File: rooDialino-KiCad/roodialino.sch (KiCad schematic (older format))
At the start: 49 parts, among them J1 Raspi Connector, J2 ICSP, J3 FTDI, J4 IR Receiver, J5 IR LED, Q1 2N7002, Q2 2N7002, Q3 2N7002, SW1 SW_Push, U1 ATmega328P, U2 TSOP312xx, U3 TXS0108EPW, Y1 16MHz

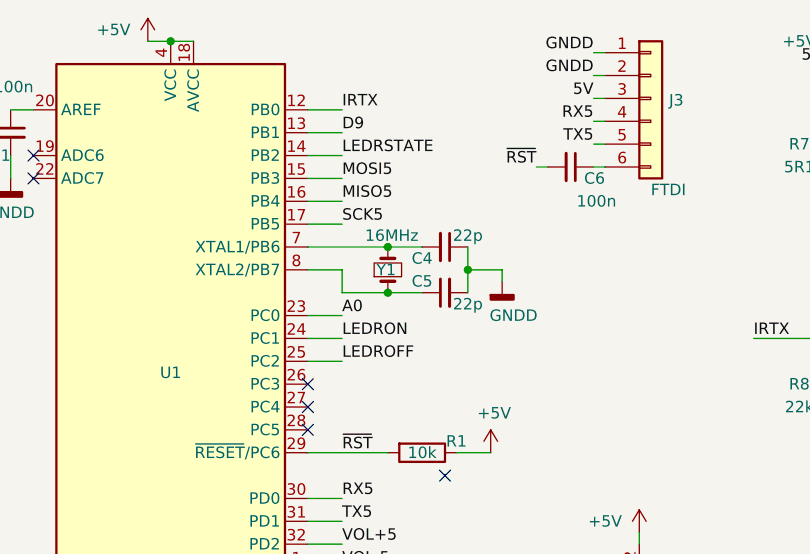
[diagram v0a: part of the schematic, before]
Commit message: Fixing the crystal footprint
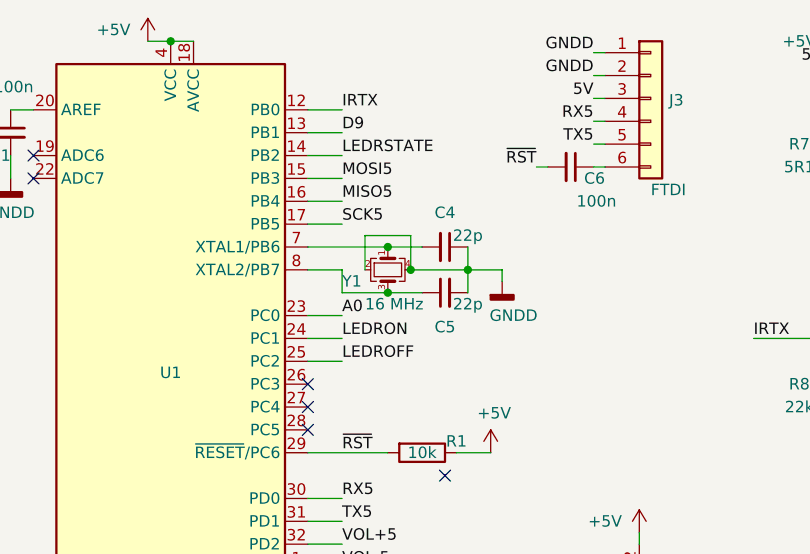
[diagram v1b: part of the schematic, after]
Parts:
- removed Y1: 16MHz, Crystal:Crystal_SMD_3225-4Pin_3.2x2.5mm, symbol Device:Crystal_Small
- added Y1: 16 MHz, Crystal:Crystal_SMD_3225-4Pin_3.2x2.5mm, symbol Device:Crystal_GND24_Small
- C11: LCSC (none) -> C1622
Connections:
- net GNDD: now also Y1.2, Y1.4
- net at C4.2, U1.7 (XTAL1/PB6): now also Y1.1
- net at C5.1, U1.8 (XTAL2/PB7): now also Y1.3
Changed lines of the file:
@@
 Wire Wire Line
 	700  1100 800  1100
-$Comp
-L Device:Crystal_Small Y1
-U 1 1 5E11C8C9
-P 2350 1800
-F 0 "Y1" V 2350 1750 50  0000 L CNN
-F 1 "16MHz" V 2500 1700 50  0000 L CNN
-F 2 "Crystal:Crystal_SMD_3225-4Pin_3.2x2.5mm" H 2350 1800 50  0001 C CNN
-F 3 "~" H 2350 1800 50  0001 C CNN
-F 4 "C13738" V 2350 1800 50  0001 C CNN "LCSC"
-	1    2350 1800
-	0    1    -1   0
-$EndComp
-Wire Wire Line
-	2000 1700 2350 1700
-Wire Wire Line
-	2350 1700 2500 1700
-Connection ~ 2350 1700
 Wire Wire Line
 	2700 1700 2700 1800
 Wire Wire Line
-	2350 1900 2500 1900
-Wire Wire Line
 	2000 1800 2150 1800
 Wire Wire Line
 	2150 1800 2150 1900
-Wire Wire Line
-	2150 1900 2350 1900
-Connection ~ 2350 1900
 $Comp
 L Device:C_Small C4
 U 1 1 5E11A53A
 P 2600 1700
-F 0 "C4" V 2650 1600 50  0000 C CNN
+F 0 "C4" V 2450 1700 50  0000 C CNN
 F 1 "22p" V 2550 1800 50  0000 C CNN
 F 2 "Capacitor_SMD:C_0402_1005Metric" H 2600 1700 50  0001 C CNN
@@
 U 1 1 5E11B014
 P 2600 1900
-F 0 "C5" V 2550 2000 50  0000 C CNN
+F 0 "C5" V 2750 1900 50  0000 C CNN
 F 1 "22p" V 2650 1800 50  0000 C CNN
 F 2 "Capacitor_SMD:C_0402_1005Metric" H 2600 1900 50  0001 C CNN
@@
 F 2 "Capacitor_SMD:C_0603_1608Metric" H 6050 6900 50  0001 C CNN
 F 3 "~" H 6050 6900 50  0001 C CNN
+F 4 "C1622" H 6050 6900 50  0001 C CNN "LCSC"
 	1    6050 6900
 	-1   0    0    1
@@
 NoConn ~ 2000 2500
 NoConn ~ 2600 2700
+$Comp
+L Device:Crystal_GND24_Small Y1
+U 1 1 617082D2
+P 2350 1800
+F 0 "Y1" V 2400 1600 50  0000 L CNN
+F 1 "16 MHz" V 2500 1700 50  0000 L CNN
+F 2 "Crystal:Crystal_SMD_3225-4Pin_3.2x2.5mm" H 2350 1800 50  0001 C CNN
+F 3 "~" H 2350 1800 50  0001 C CNN
+F 4 "C13738" V 2350 1800 50  0001 C CNN "LCSC"
+	1    2350 1800
+	0    1    1    0
+$EndComp
+Wire Wire Line
+	2150 1900 2350 1900
+Wire Wire Line
+	2000 1700 2350 1700
+Connection ~ 2350 1700
+Wire Wire Line
+	2350 1700 2500 1700
+Connection ~ 2350 1900
+Wire Wire Line
+	2350 1900 2500 1900
+Wire Wire Line
+	2700 1800 2450 1800
+Wire Wire Line
+	2250 1800 2250 1650
+Wire Wire Line
+	2250 1650 2450 1650
+Wire Wire Line
+	2450 1650 2450 1800
+Connection ~ 2450 1800
 $EndSCHEMATC

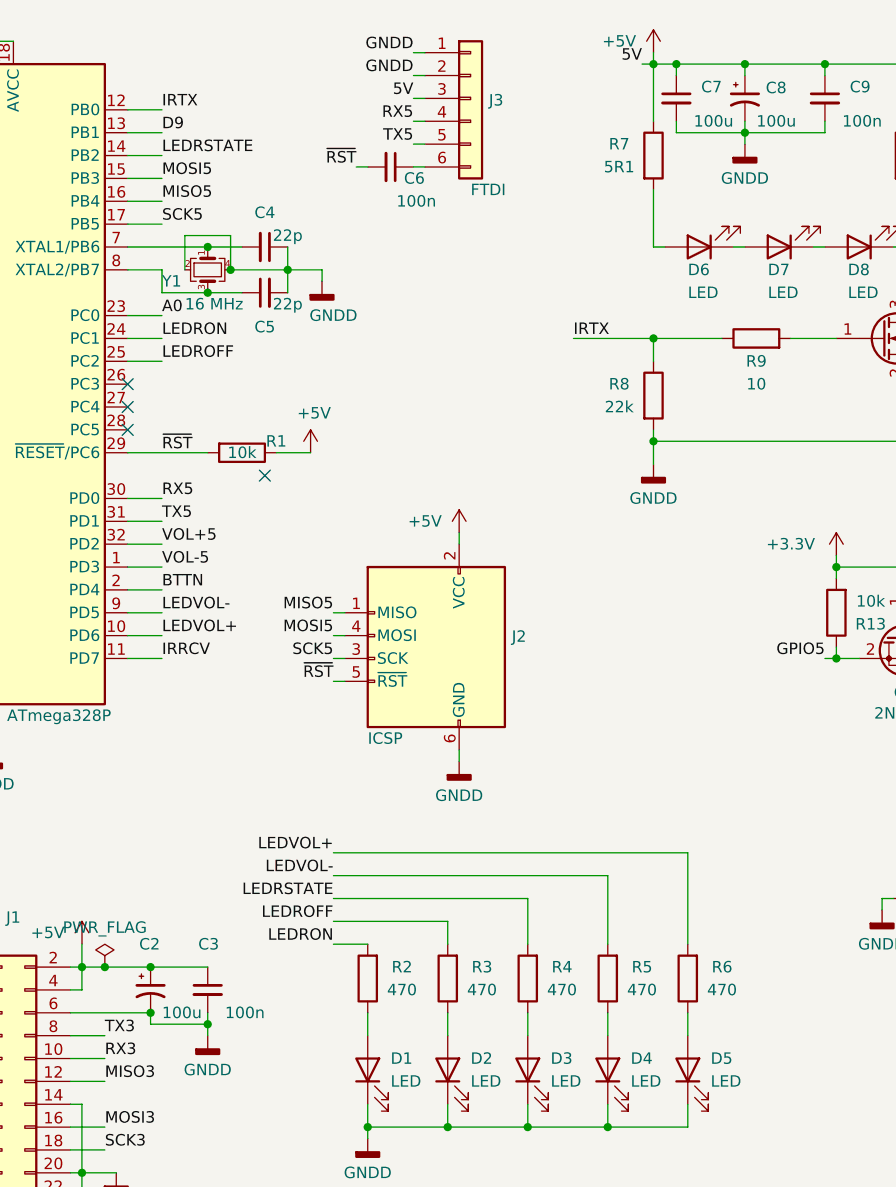
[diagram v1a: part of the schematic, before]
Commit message: Better caps, less magic smoke!
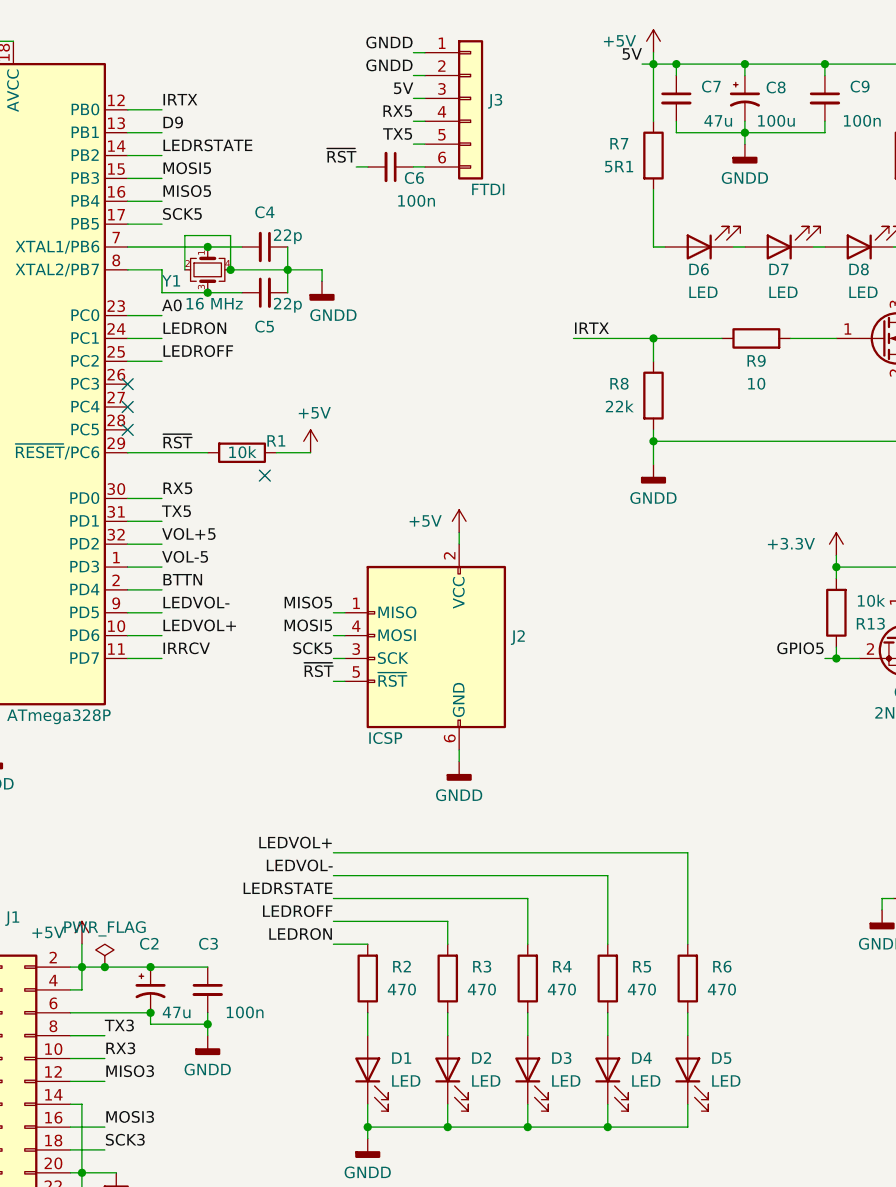
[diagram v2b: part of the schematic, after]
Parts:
- C2: value 100u -> 47u; footprint Capacitor_SMD:C_1210_3225Metric -> Capacitor_SMD:CP_Elec_4x5.8; LCSC C16133 -> C178589
- C7: value 100u -> 47u
- C8: footprint Capacitor_SMD:C_1210_3225Metric -> Capacitor_SMD:CP_Elec_4x5.8; LCSC C16133 -> C178589
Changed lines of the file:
@@
 F 0 "C8" H 4791 1096 50  0000 L CNN
 F 1 "100u" H 4750 950 50  0000 L CNN
-F 2 "Capacitor_SMD:C_1210_3225Metric" H 4700 1050 50  0001 C CNN
-F 3 "~" H 4700 1050 50  0001 C CNN
-F 4 "C16133" H 4700 1050 50  0001 C CNN "LCSC"
+F 2 "Capacitor_SMD:CP_Elec_4x5.8" H 4700 1050 50  0001 C CNN
+F 3 "https://lcsc.com/product-detail/Aluminum-Electrolytic-Capacitors---SMD_PANASONIC-EEEFT1C470AR_C178589.html" H 4700 1050 50  0001 C CNN
+F 4 "C178589" H 4700 1050 50  0001 C CNN "LCSC"
 	1    4700 1050
 	1    0    0    -1
@@
 P 2100 4950
 F 0 "C2" H 2050 5150 50  0000 L CNN
-F 1 "100u" H 2150 4850 50  0000 L CNN
-F 2 "Capacitor_SMD:C_1210_3225Metric" H 2100 4950 50  0001 C CNN
-F 3 "~" H 2100 4950 50  0001 C CNN
-F 4 "C16133" H 2100 4950 50  0001 C CNN "LCSC"
+F 1 "47u" H 2150 4850 50  0000 L CNN
+F 2 "Capacitor_SMD:CP_Elec_4x5.8" H 2100 4950 50  0001 C CNN
+F 3 "https://lcsc.com/product-detail/Aluminum-Electrolytic-Capacitors---SMD_PANASONIC-EEEFT1C470AR_C178589.html" H 2100 4950 50  0001 C CNN
+F 4 "C178589" H 2100 4950 50  0001 C CNN "LCSC"
 	1    2100 4950
 	1    0    0    -1
@@
 P 4400 1050
 F 0 "C7" H 4600 1100 50  0000 R CNN
-F 1 "100u" H 4650 950 50  0000 R CNN
+F 1 "47u" H 4650 950 50  0000 R CNN
 F 2 "Capacitor_SMD:C_1206_3216Metric" H 4400 1050 50  0001 C CNN
-F 3 "~" H 4400 1050 50  0001 C CNN
+F 3 "https://datasheet.lcsc.com/lcsc/1810301816_Samsung-Electro-Mechanics-CL31A107MQHNNNE_C15008.pdf" H 4400 1050 50  0001 C CNN
 F 4 "C15008" H 4400 1050 50  0001 C CNN "LCSC"
 	1    4400 1050

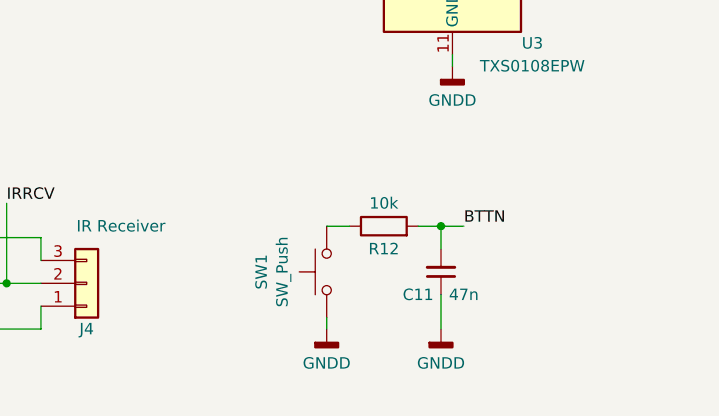
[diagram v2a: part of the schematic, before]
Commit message: Removing debounce RC
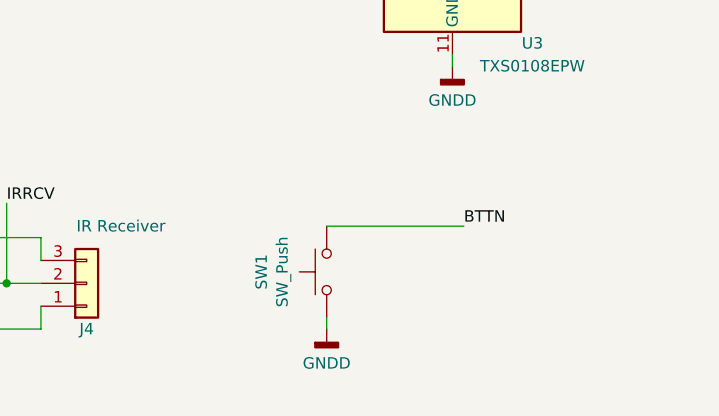
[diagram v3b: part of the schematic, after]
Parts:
- removed C11: 47n, Capacitor_SMD:C_0603_1608Metric, symbol Device:C_Small
- removed R12: 10k, Resistor_SMD:R_0402_1005Metric, symbol Device:R
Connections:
- net BTTN: now also SW1.2
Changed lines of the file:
@@
 VOL+5
-$Comp
-L Device:R R12
-U 1 1 6169CA12
-P 5800 6700
-F 0 "R12" V 5700 6700 50  0000 C CNN
-F 1 "10k" V 5900 6700 50  0000 C CNN
-F 2 "Resistor_SMD:R_0402_1005Metric" V 5730 6700 50  0001 C CNN
-F 3 "~" H 5800 6700 50  0001 C CNN
-F 4 "C25744" V 5800 6700 50  0001 C CNN "LCSC"
-	1    5800 6700
-	0    -1   -1   0
-$EndComp
-$Comp
-L Device:C_Small C11
-U 1 1 6169CEA6
-P 6050 6900
-F 0 "C11" H 6150 7000 50  0000 C CNN
-F 1 "47n" H 5950 7000 50  0000 C CNN
-F 2 "Capacitor_SMD:C_0603_1608Metric" H 6050 6900 50  0001 C CNN
-F 3 "~" H 6050 6900 50  0001 C CNN
-F 4 "C1622" H 6050 6900 50  0001 C CNN "LCSC"
-	1    6050 6900
-	-1   0    0    1
-$EndComp
-$Comp
-L power:GNDD #PWR023
-U 1 1 6169EC89
-P 6050 7150
-F 0 "#PWR023" H 6050 6900 50  0001 C CNN
-F 1 "GNDD" H 6050 7000 50  0000 C CNN
-F 2 "" H 6050 7150 50  0001 C CNN
-F 3 "" H 6050 7150 50  0001 C CNN
-	1    6050 7150
-	1    0    0    -1
-$EndComp
-Wire Wire Line
-	5950 6700 6050 6700
-Wire Wire Line
-	6050 6700 6050 6800
 $Comp
 L Switch:SW_Push SW1
@@
 $EndComp
 Wire Wire Line
-	5550 6700 5650 6700
-Wire Wire Line
-	6050 7000 6050 7150
-Wire Wire Line
 	5550 7150 5550 7100
 $Comp
@@
 F 1 "LED" V 3000 5200 50  0000 R CNN
 F 2 "LED_SMD:LED_0603_1608Metric" H 3050 5300 50  0001 C CNN
-F 3 "~" H 3050 5300 50  0001 C CNN
+F 3 "https://datasheet.lcsc.com/lcsc/1811101510_Everlight-Elec-19-217-BHC-ZL1M2RY-3T_C72041.pdf" H 3050 5300 50  0001 C CNN
 F 4 "C72041" V 3050 5300 50  0001 C CNN "LCSC"
 	1    3050 5300
@@
 F 1 "LED" V 3350 5200 50  0000 R CNN
 F 2 "LED_SMD:LED_0603_1608Metric" H 3400 5300 50  0001 C CNN
-F 3 "~" H 3400 5300 50  0001 C CNN
+F 3 "https://datasheet.lcsc.com/lcsc/1811101510_Everlight-Elec-19-217-BHC-ZL1M2RY-3T_C72041.pdf" H 3400 5300 50  0001 C CNN
 F 4 "C72041" V 3400 5300 50  0001 C CNN "LCSC"
 	1    3400 5300
@@
 F 1 "LED" V 3700 5200 50  0000 R CNN
 F 2 "LED_SMD:LED_0603_1608Metric" H 3750 5300 50  0001 C CNN
-F 3 "~" H 3750 5300 50  0001 C CNN
+F 3 "https://datasheet.lcsc.com/lcsc/1811101510_Everlight-Elec-19-217-BHC-ZL1M2RY-3T_C72041.pdf" H 3750 5300 50  0001 C CNN
 F 4 "C72041" V 3750 5300 50  0001 C CNN "LCSC"
 	1    3750 5300
@@
 Text Label 6150 6700 0    50   ~ 0
 BTTN
-Wire Wire Line
-	6150 6700 6050 6700
-Connection ~ 6050 6700
 Text Label 1100 6250 2    50   ~ 0
 GPIO5
@@
 	2450 1650 2450 1800
 Connection ~ 2450 1800
+Wire Wire Line
+	5550 6700 6150 6700
 $EndSCHEMATC

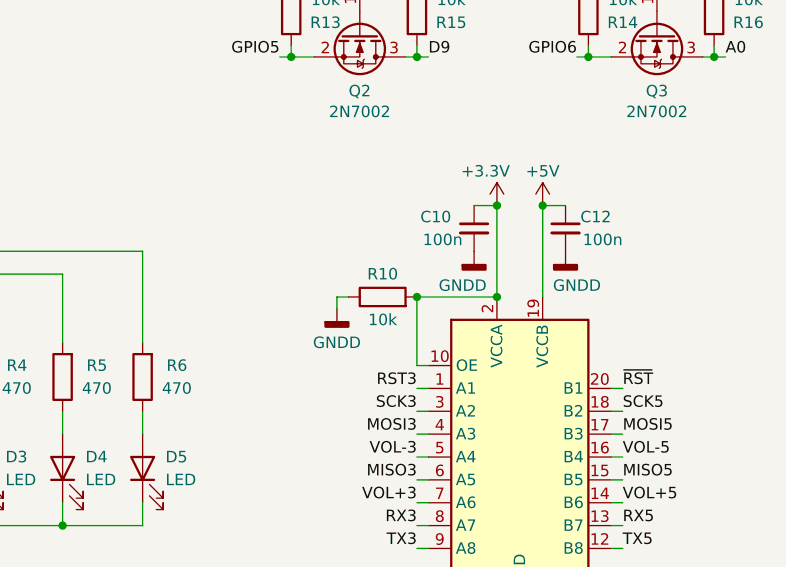
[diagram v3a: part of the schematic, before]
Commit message: Levelshifter's OE gets permanently enabled. No need to ever have it low.
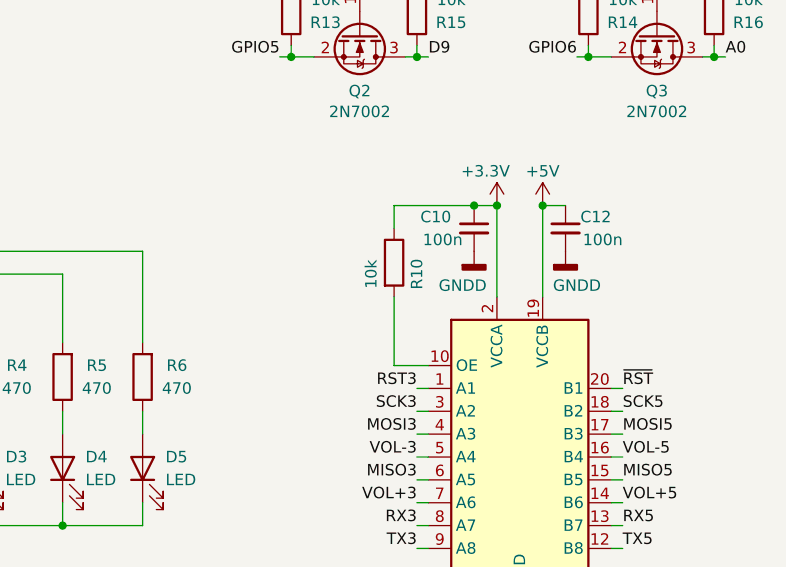
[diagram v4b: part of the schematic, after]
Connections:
- net +3V3: now also R10.1; no longer R10.2, U3.10 (OE)
- net GNDD: no longer R10.1
- new net: R10.2, U3.10 (OE)
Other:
- moved on the sheet: R10
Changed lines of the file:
@@
 $EndComp
 Wire Wire Line
-	5700 4850 5650 4850
-Wire Wire Line
-	5650 4850 5650 4550
-Wire Wire Line
-	5650 4550 6000 4550
-Connection ~ 6000 4550
+	5700 4850 5550 4850
+Wire Wire Line
+	5550 4850 5550 4550
 Wire Wire Line
 	5700 4950 5650 4950
@@
 L Device:R R10
 U 1 1 61FCB007
-P 5500 4550
-F 0 "R10" V 5600 4550 50  0000 C CNN
-F 1 "10k" V 5400 4550 50  0000 C CNN
-F 2 "Resistor_SMD:R_0402_1005Metric" V 5430 4550 50  0001 C CNN
-F 3 "~" H 5500 4550 50  0001 C CNN
-F 4 "C25744" V 5500 4550 50  0001 C CNN "LCSC"
-	1    5500 4550
-	0    -1   -1   0
-$EndComp
-Connection ~ 5650 4550
-$Comp
-L power:GNDD #PWR019
-U 1 1 61FCD646
-P 5300 4600
-F 0 "#PWR019" H 5300 4350 50  0001 C CNN
-F 1 "GNDD" H 5300 4450 50  0000 C CNN
-F 2 "" H 5300 4600 50  0001 C CNN
-F 3 "" H 5300 4600 50  0001 C CNN
-	1    5300 4600
-	1    0    0    -1
-$EndComp
-Wire Wire Line
-	5300 4600 5300 4550
-Wire Wire Line
-	5300 4550 5350 4550
+P 5550 4400
+F 0 "R10" V 5650 4350 50  0000 C CNN
+F 1 "10k" V 5450 4350 50  0000 C CNN
+F 2 "Resistor_SMD:R_0402_1005Metric" V 5480 4400 50  0001 C CNN
+F 3 "~" H 5550 4400 50  0001 C CNN
+F 4 "C25744" V 5550 4400 50  0001 C CNN "LCSC"
+	1    5550 4400
+	1    0    0    -1
+$EndComp
 Wire Wire Line
 	6100 5950 6100 6000
@@
 Wire Wire Line
 	5550 6700 6150 6700
+Wire Wire Line
+	5550 4250 5550 4150
+Wire Wire Line
+	5550 4150 5900 4150
+Connection ~ 5900 4150
 $EndSCHEMATC
